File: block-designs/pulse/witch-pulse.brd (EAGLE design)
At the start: 134.6 x 64.4 mm, 18 parts, among them IC1 74LS73N, IC2 74S08N

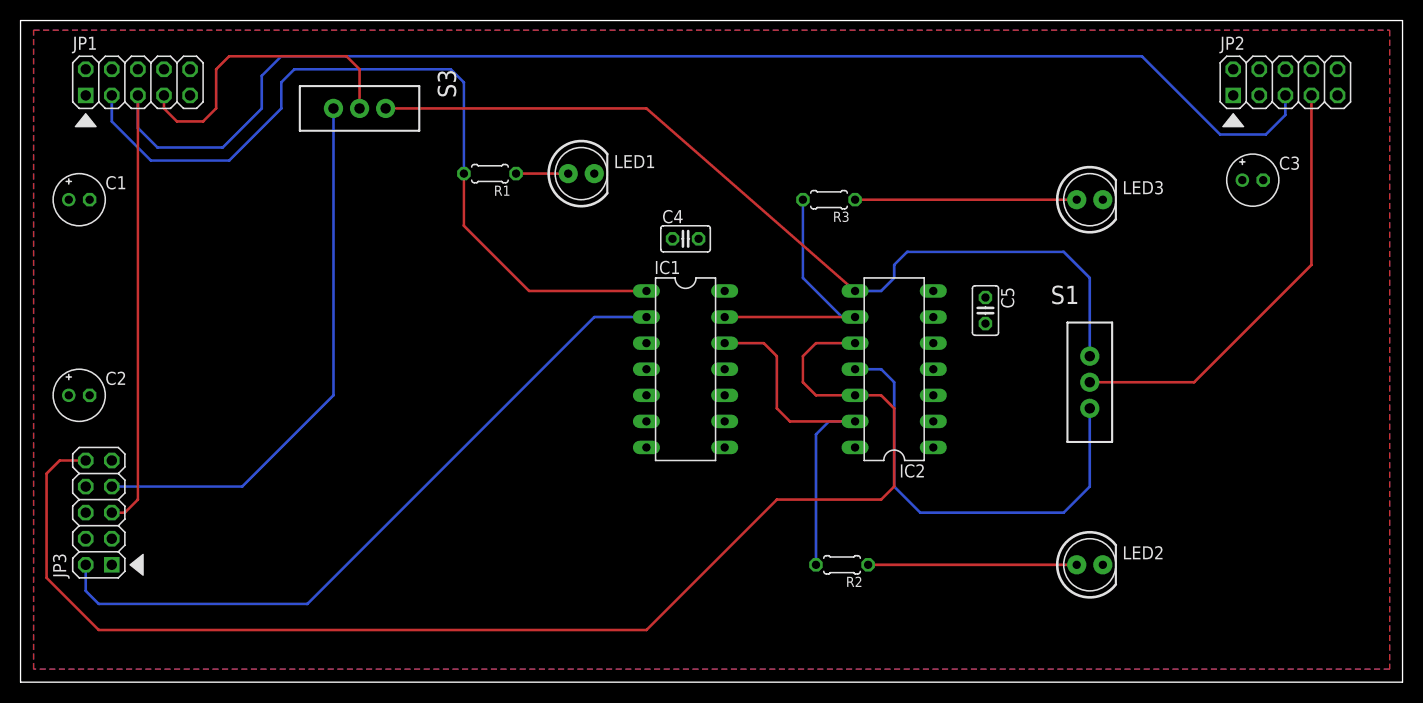
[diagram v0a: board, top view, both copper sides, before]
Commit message: updated schematics and layouts for phase 1 block designs
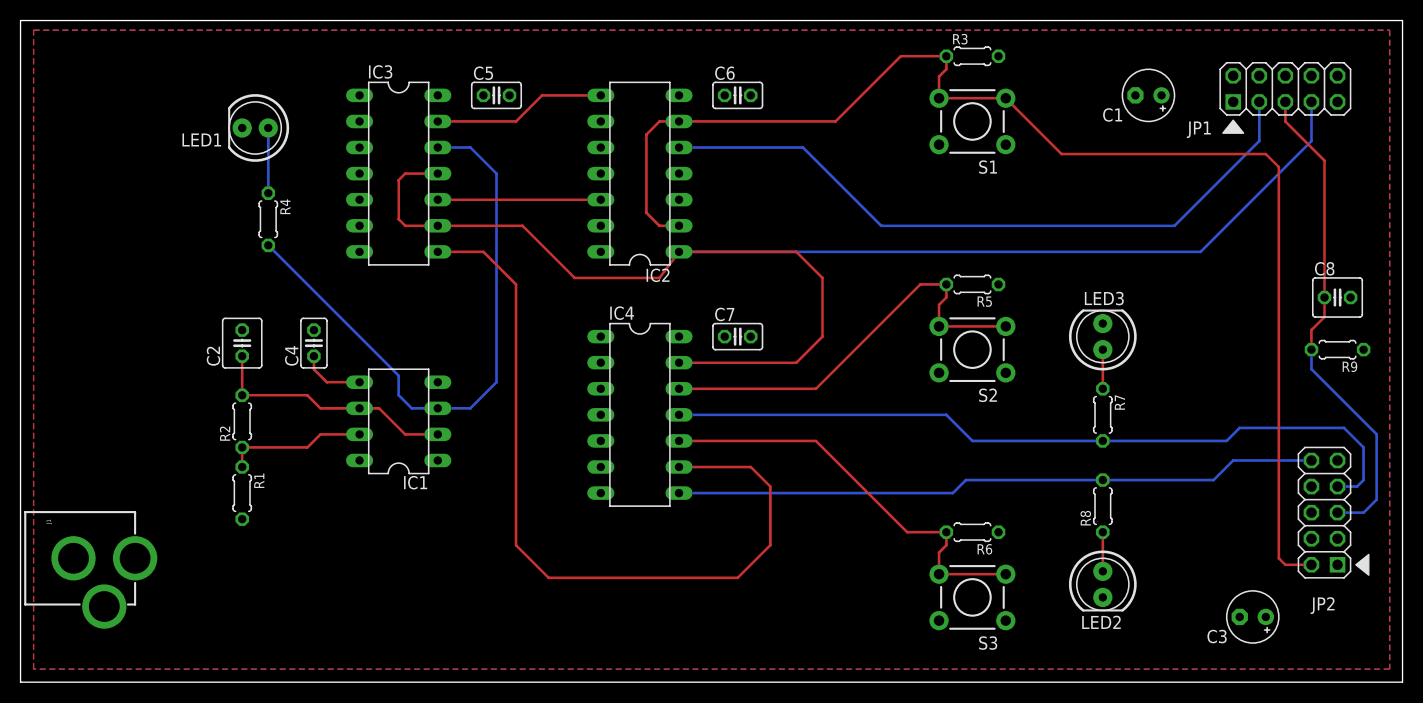
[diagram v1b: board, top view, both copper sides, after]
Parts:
- removed JP3: (no value), pinhead:2X05
- added C6, C7: (no value), resistor:C025-025X050
- added C8: (no value), resistor:C025-040X050
- added IC3: 74S08N, 74xx-us:DIL14
- added IC4: 7432N, 74xx-us:DIL14
- added J1: POWER_JACKPTH, SparkFun-Connectors:POWER_JACK_PTH
- added R4, R7, R8: 330R, resistor:0204/5
- added R5, R6, R9: (no value), resistor:0204/5
- added S2: (no value), SparkFun-Electromechanical:TACTILE-PTH
- C1, C3: device resistor:E2-5 -> resistor:E2,5-5
- C2: device resistor:E2-5 -> resistor:C025-040X050
- IC1: value 74LS73N -> NE555; device 74xx-us:DIL14 -> st-microelectronics:DIL-08
- IC2: value 74S08N -> 74LS73N
- R1, R2, R3: value 330R -> (none)
- S1, S3: device SparkFun-Electromechanical:SWITCH-SPDT -> SparkFun-Electromechanical:TACTILE-PTH
- moved JP1 111.8 mm to (123.2, 57.8)
- moved C1 104.6 mm to (109.9, 57.1), turned to 180 degrees
- moved S3 76.4 mm to (92.7, 8.26), turned to 180 degrees
- moved R2 60.1 mm to (21.6, 25.4), turned to 90 degrees
- moved C5 52.0 mm to (46.4, 57.1), turned to 0 degrees
- moved C3 42.5 mm to (120.0, 6.35), turned to 180 degrees
- moved JP2 42.1 mm to (127.0, 16.5), turned to 90 degrees
- moved R1 39.4 mm to (21.6, 18.4), turned to 270 degrees
- moved C4 37.6 mm to (28.6, 33.0), turned to 90 degrees
- moved LED1 32.1 mm to (22.9, 54.0), turned to 180 degrees
- moved IC2 31.2 mm to (60.3, 49.5)
- moved IC1 28.4 mm to (36.8, 25.4), turned to 90 degrees
- moved S1 27.9 mm to (92.7, 54.6), turned to 180 degrees
- moved R3 19.8 mm to (92.7, 61.0), turned to 0 degrees
- moved C2 16.7 mm to (21.6, 33.0), turned to 90 degrees
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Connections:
- removed net N$1: JP2.7, S1.2
- removed net N$3: IC1.13, IC2.9, R3.2
- removed net N$32: JP1.5, JP2.5, JP3.5
- removed net N$43: IC2.8, S1.1, S3.1
- removed net N$8: LED1.A, R1.1
- removed net TRANSFER_PULSE: JP1.7, S3.2
- removed net ZC_TX: IC1.1, JP1.3, R1.2
- new net 10A_PULSE: IC2.1, IC3.11, IC3.9, IC4.13, JP1.7
- new net 9A_PULSE: IC3.8, IC4.9
- new net DK_RESET: C8.1, JP1.5, JP2.5, R9.2
- new net N$12: IC2.5, JP1.3
- new net N$13: C2.1, IC1.2, IC1.6, R2.2
- new net N$14: C4.1, IC1.5
- new net N$15: LED1.A, R4.1
- new net N$17: LED3.A, R7.1
- new net N$18: LED2.A, R8.1
- new net N$19: IC4.11, JP2.7, R7.2
- new net RESET: IC2.2, IC2.6, JP2.2, R3.1, S1.3, S1.4
- net N$10: now also IC1.7, R1.1, R2.1; no longer IC1.2, JP3.2
- net N$2: now also IC1.3, IC3.12, R4.2; no longer IC2.10, IC2.12, JP3.10
- net N$4: now also IC4.8, JP2.10, R8.2; no longer IC1.12, IC2.13, R2.2
- net N$5: now also IC2.8, IC3.13; no longer IC2.11, S1.3
- net N$6: now also IC4.12, R5.2, S2.3, S2.4; no longer LED2.A, R2.1
- net N$7: now also IC2.12, IC3.10; no longer LED3.A, R3.1
- net N$9: now also IC4.10, R6.2, S3.4; no longer JP3.7
- net VDD: now also C6.1, C7.1, IC1.8, IC2.4, IC2.7, IC3.14, IC4.14, J1.PWR, R1.2, R3.2, R9.1, S2.1, S2.2, S3.1, S3.2; no longer C2.+, C4.1, IC1.14, JP3.1
- net VSS: now also C2.2, C6.2, C7.2, C8.2, IC1.1, IC2.10, IC2.11, IC2.3, IC3.7, IC4.7, J1.GNDBREAK, R5.1, R6.1, S1.1, S1.2; no longer C2.-, IC1.11, IC1.3, IC2.7, JP3.9
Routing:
- net N$32: track 169.6 -> 0.00 mm
- net 10A_PULSE: track 0.00 -> 144.5 mm
- net RESET: track 0.00 -> 125.5 mm
- net N$43: track 86.3 -> 0.00 mm
- net ZC_TX: track 78.5 -> 0.00 mm
- net 9A_PULSE: track 0.00 -> 77.1 mm
- net N$19: track 0.00 -> 75.0 mm
- net N$2: track 130.6 -> 58.1 mm
- net N$12: track 0.00 -> 66.9 mm
- net N$10: track 69.2 -> 13.9 mm
- net DK_RESET: track 0.00 -> 47.8 mm
- net N$1: track 42.8 -> 0.00 mm
- net TRANSFER_PULSE: track 30.0 -> 0.00 mm
- net N$4: track 35.9 -> 62.9 mm
- net N$3: track 27.0 -> 0.00 mm
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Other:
- board text removed: "ADD"
- board text removed: "CLEAR"
- board text removed: "COMP"
- board text removed: "PULSE GENERATOR"
- board text removed: "RECEIVE"
- board text removed: "SEND"
- board text removed: "ZC"
